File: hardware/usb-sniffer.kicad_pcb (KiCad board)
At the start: 2 copper layers, 58.2 x 38.1 mm, 86 parts, among them IC1 LCMXO2-2000HC-5TG100, IC10 DSC6101CI2A-024.0000, IC2 MIC5504-3.3v, IC3 MAX9032AKA+T, IC4 USB3343, IC5 MAX9032AKA+T, IC6 DSC6101CI2A-026.0000, IC7 MAX9032AKA+T, IC8 24LC128, IC9 CY7C68013A-56PVXC, J1 USB-C, J2 USB-C, J3 USB-A, J4 IN

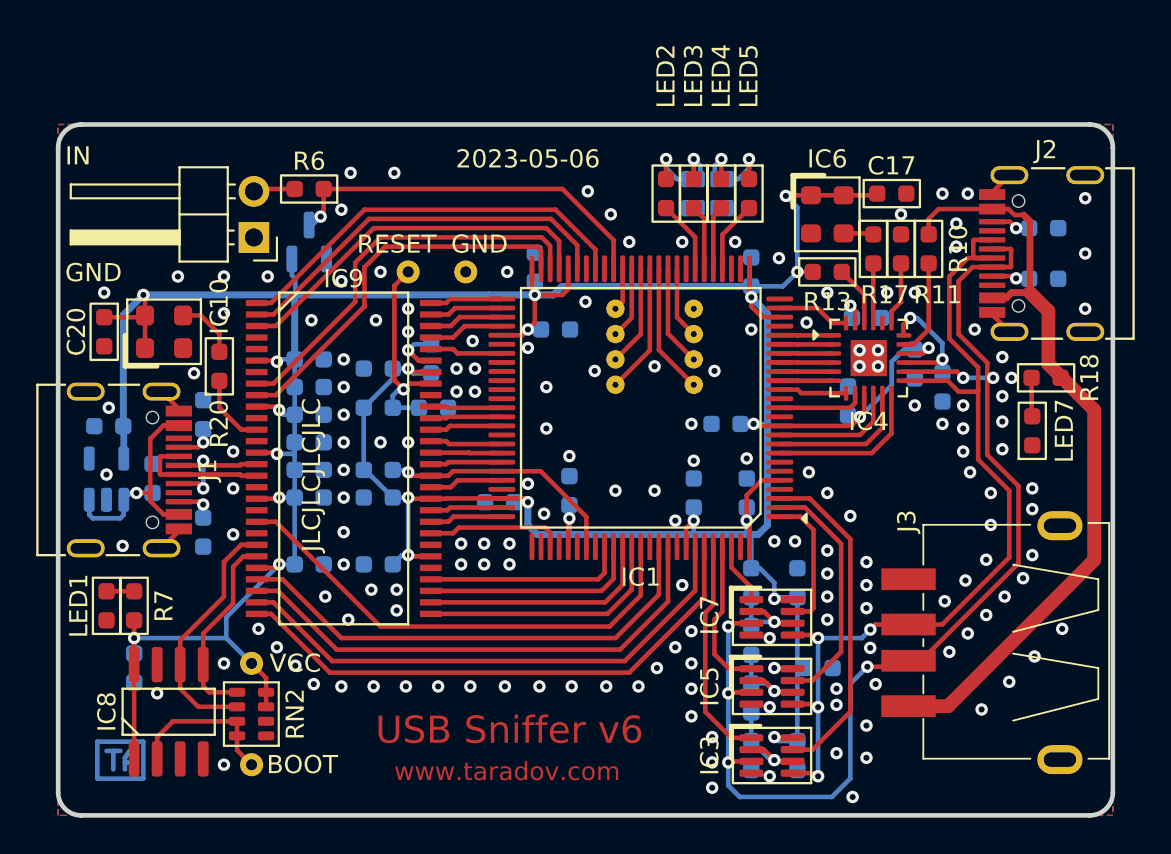
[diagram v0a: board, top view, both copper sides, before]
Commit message: Use LED_SMD:LED_0603_1608Metric footprint for LEDs
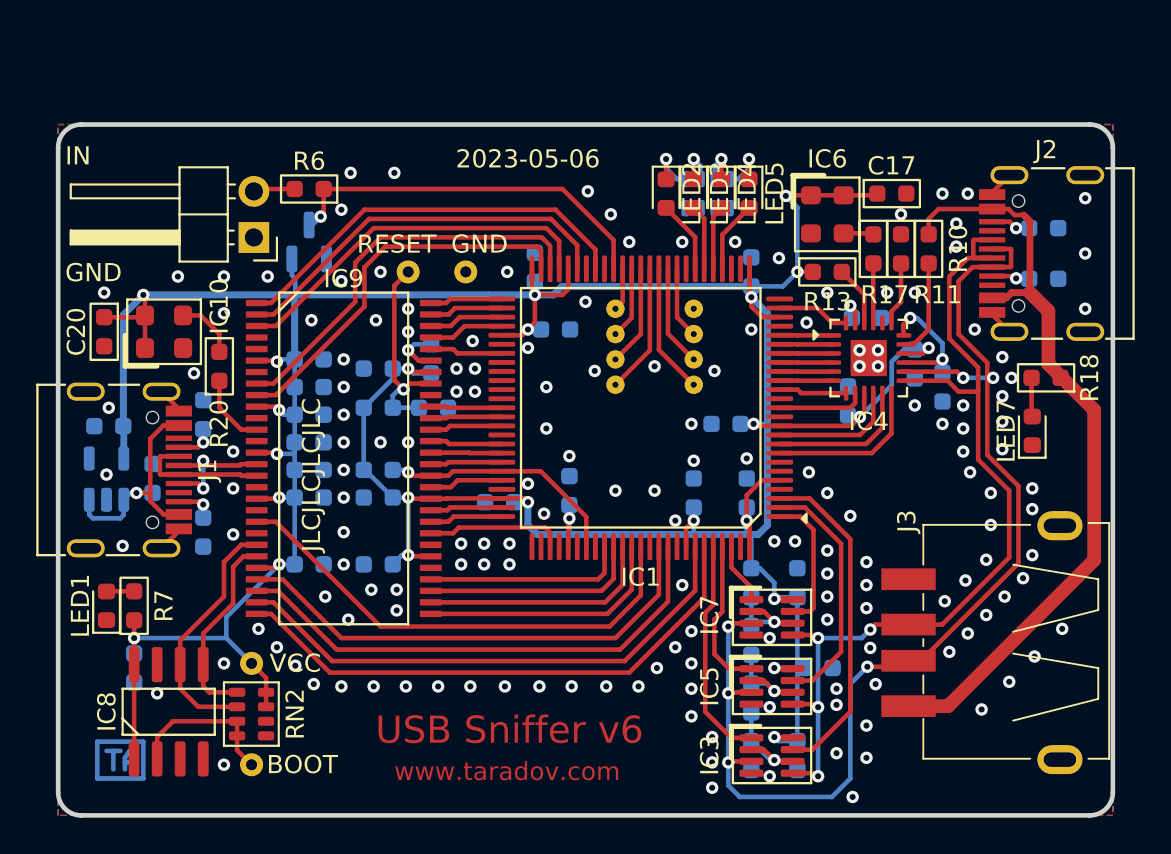
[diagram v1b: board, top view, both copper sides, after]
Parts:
- LED1, LED2, LED3, LED4, LED5, LED7: footprint ataradov_smd:0603 -> LED_SMD:LED_0603_1608Metric
